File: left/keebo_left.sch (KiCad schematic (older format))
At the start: 57 parts, among them J0 Conn_01x01, SW1 SW_Push, SW10 SW_Push, SW11 SW_Push, SW12 SW_Push, SW13 SW_Push, SW14 SW_Push, SW17 SW_Push, SW18 SW_Push, SW19 SW_Push, SW2 SW_Push, SW20 SW_Push, SW21 SW_Push, SW22 SW_Push, SW25 SW_Push, SW26 SW_Push, SW27 SW_Push, SW28 SW_Push, SW29 SW_Push, SW3 SW_Push, SW30 SW_Push, SW35 SW_Push, SW36 SW_Push, SW37 SW_Push, SW4 SW_Push, SW5 SW_Push, SW6 SW_Push, SW7 SW_Push, SW9 SW_Push

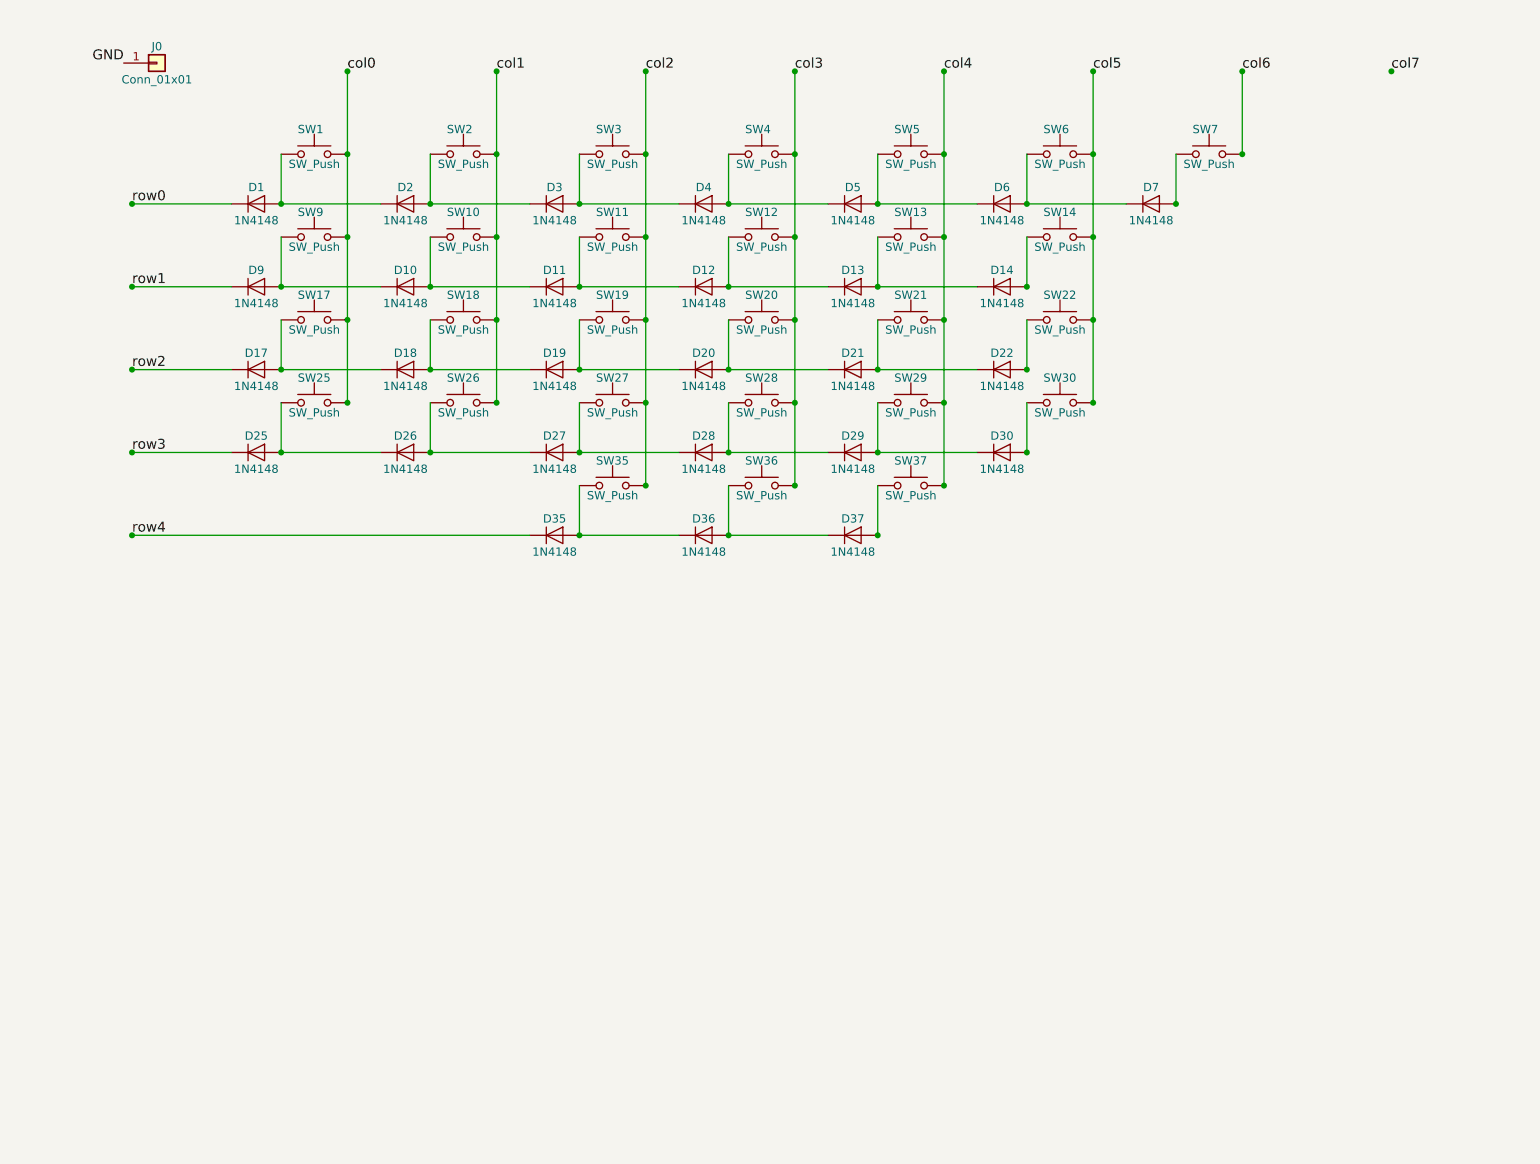
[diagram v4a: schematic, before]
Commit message: Create left board using new switch footprints
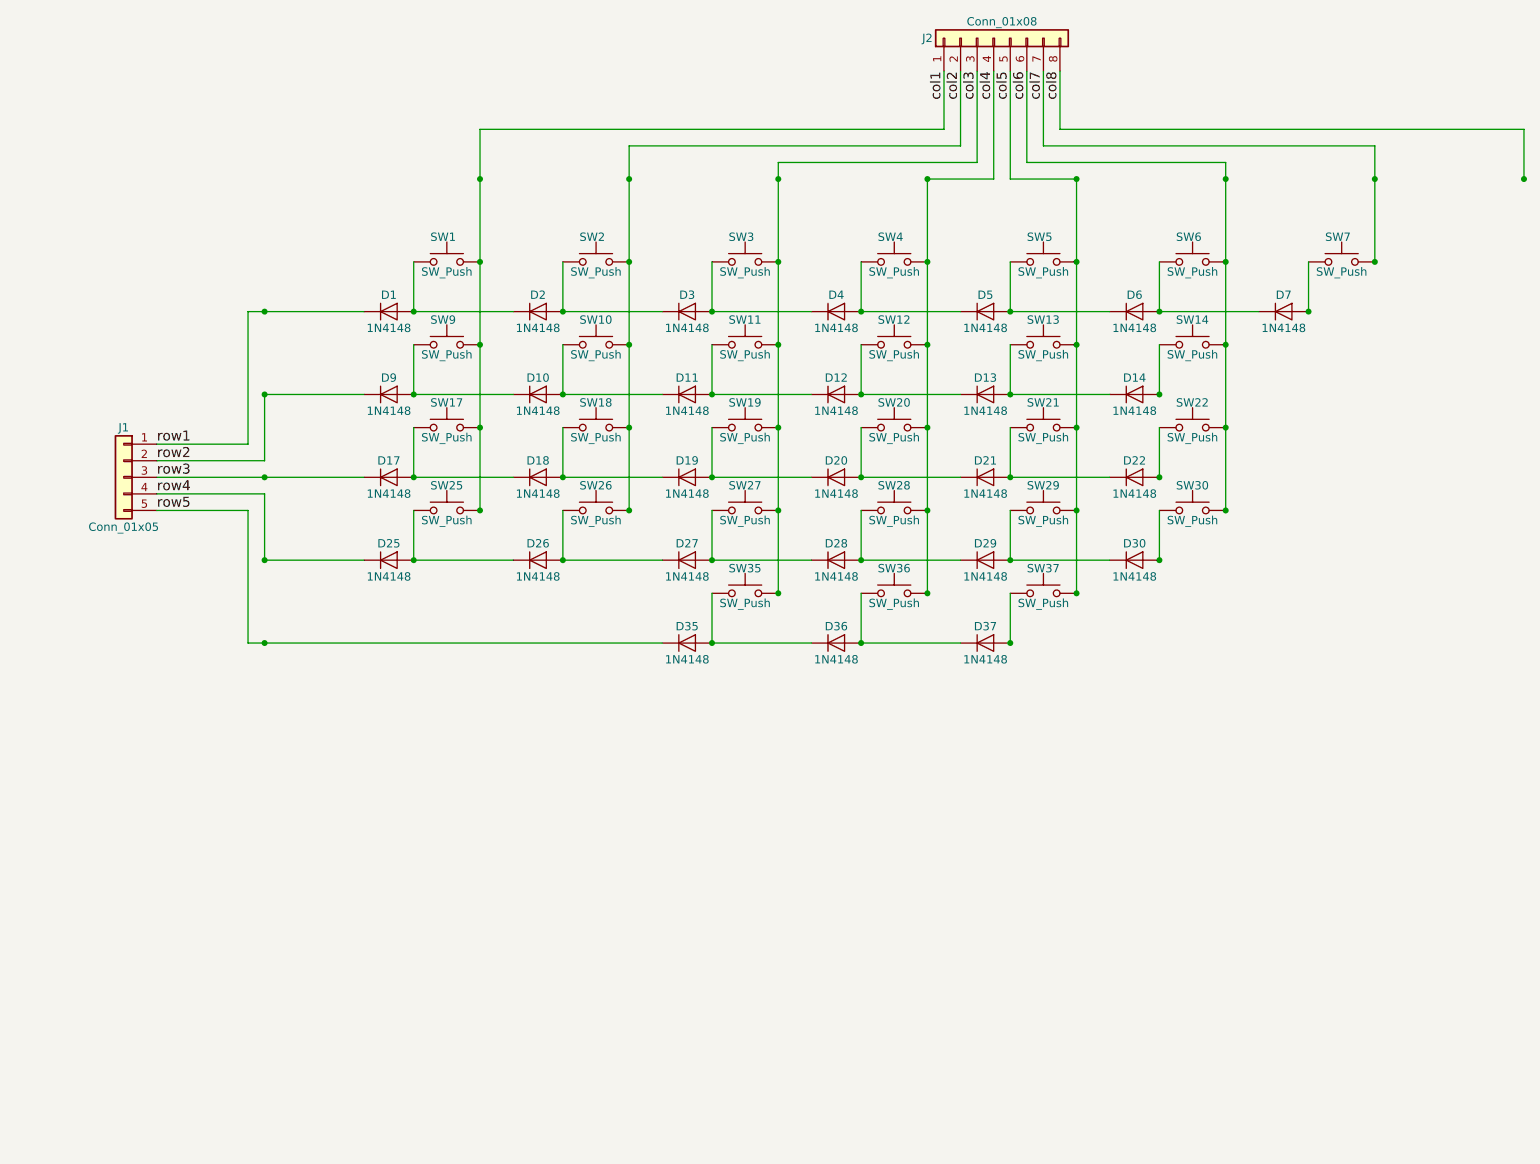
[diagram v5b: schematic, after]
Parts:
- removed J0: Conn_01x01, Mounting_Holes:MountingHole_3mm_Pad, symbol Conn_01x01
- added J1: Conn_01x05, kbo_pads:2mm_Pads_01x05, symbol Conn_01x05
- added J2: Conn_01x08, kbo_pads:2mm_Pads_01x08, symbol Conn_01x08
- SW1, SW10, SW11, SW12, SW13, SW14, SW18, SW19, SW2, SW20, SW21, SW22, SW26, SW27, SW28, SW29, SW3, SW30, SW4, SW5, SW6, SW7: footprint req:Mx_Alps_100 -> kbo_mx_lp_3d:KeeboHR_100_MX_LP
- SW17: footprint req:Mx_Alps_175 -> kbo_mx_lp_3d:KeeboHR_175_MX_LP
- SW25: footprint req:Mx_Alps_225 -> kbo_mx_lp_3d:KeeboHR_225_MX_LP
- SW35, SW36, SW37: footprint req:Mx_Alps_125 -> kbo_mx_lp_3d:KeeboHR_125_MX_LP
- SW9: footprint req:Mx_Alps_150 -> kbo_mx_lp_3d:KeeboHR_150_MX_LP
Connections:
- net col0 is gone; now on net col1: SW1.2, SW17.2, SW25.2, SW9.2
- net row0 is gone; now on net row1: D1.1 (K)
- net col1: now also J2.1 (Pin_1); no longer SW10.2, SW18.2, SW2.2, SW26.2
- net col2: now also SW10.2, SW18.2, SW2.2, SW26.2, J2.2 (Pin_2); no longer SW11.2, SW19.2, SW27.2, SW3.2, SW35.2
- net col3: now also SW11.2, SW19.2, SW27.2, SW3.2, SW35.2, J2.3 (Pin_3); no longer SW12.2, SW20.2, SW28.2, SW36.2, SW4.2
- net col4: now also SW12.2, SW20.2, SW28.2, SW36.2, SW4.2, J2.4 (Pin_4); no longer SW13.2, SW21.2, SW29.2, SW37.2, SW5.2
- net col5: now also SW13.2, SW21.2, SW29.2, SW37.2, SW5.2, J2.5 (Pin_5); no longer SW14.2, SW22.2, SW30.2, SW6.2
- net col6: now also SW14.2, SW22.2, SW30.2, SW6.2, J2.6 (Pin_6); no longer SW7.2
- net col7: now also SW7.2, J2.7 (Pin_7)
- net row1: now also J1.1 (Pin_1); no longer D9.1 (K)
- net row2: now also D9.1 (K), J1.2 (Pin_2); no longer D17.1 (K)
- net row3: now also D17.1 (K), J1.3 (Pin_3); no longer D25.1 (K)
- net row4: now also D25.1 (K), J1.4 (Pin_4); no longer D35.1 (K)
- new net col8: J2.8 (Pin_8)
- new net row5: D35.1 (K), J1.5 (Pin_5)
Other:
- moved on the sheet: D1, D10, D11, D12, D13, D14, D17, D18, D19, D2, D20, D21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

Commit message: Fix key matrix; use MX exclusively; Fix MX missing side holes.
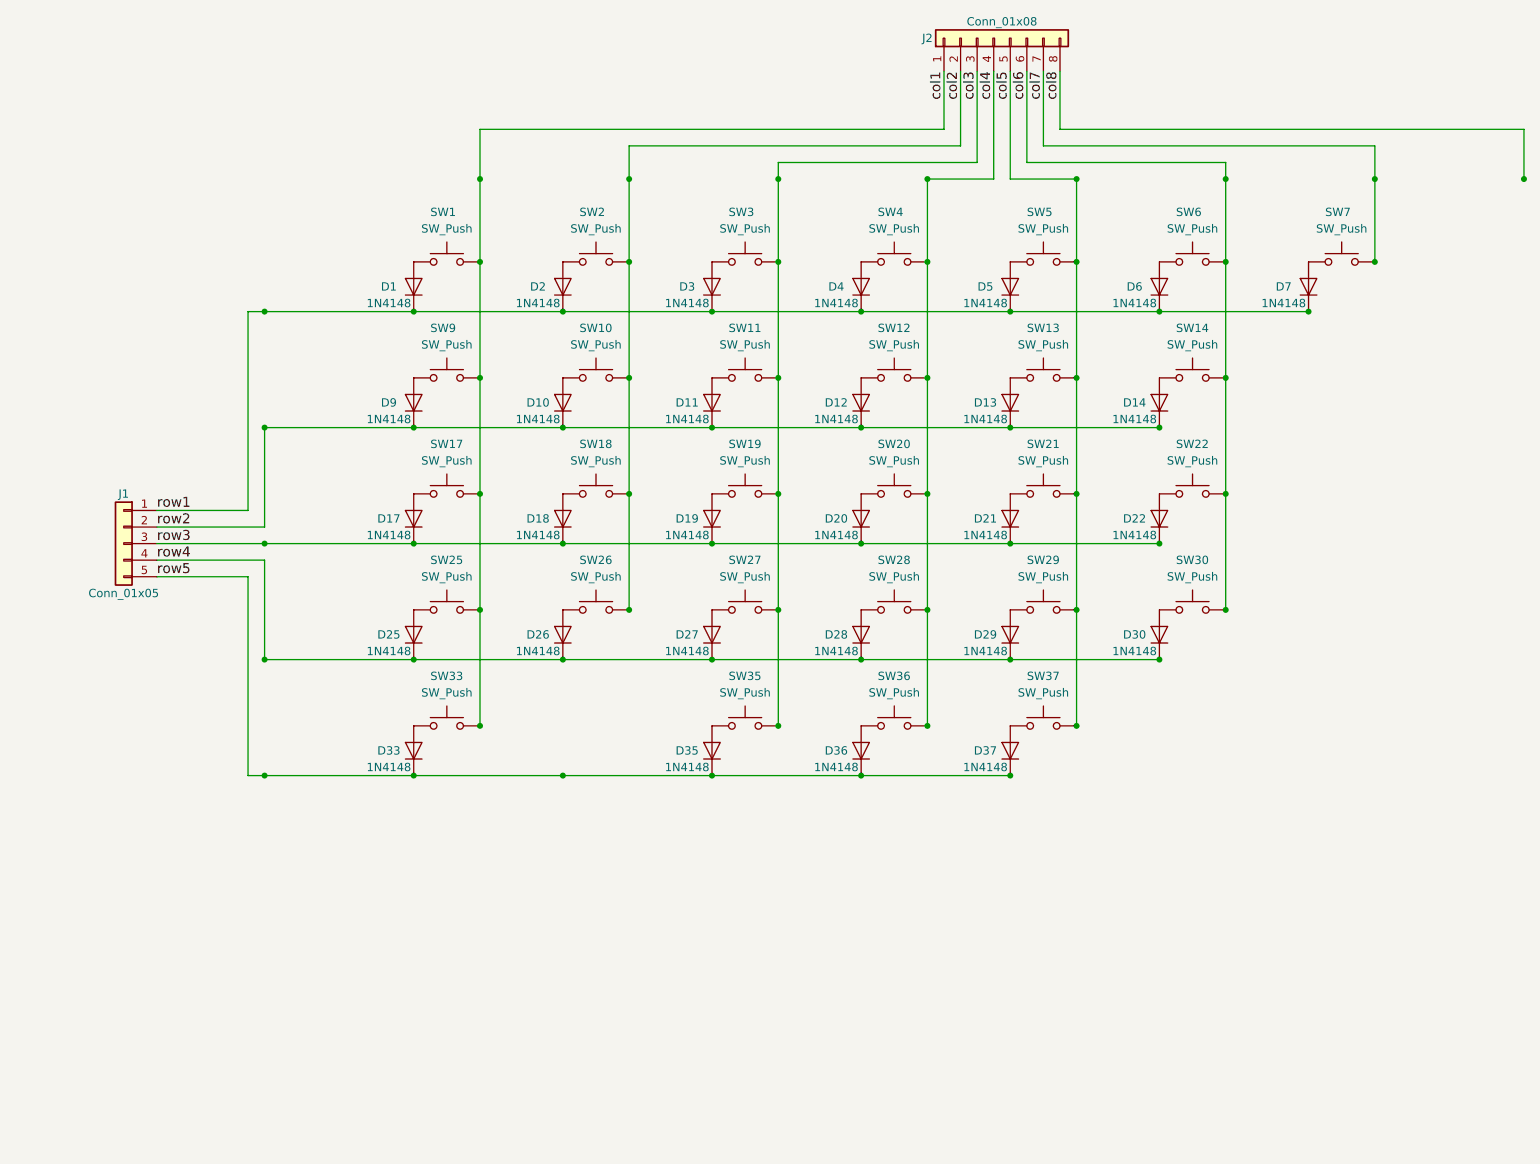
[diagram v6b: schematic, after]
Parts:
- added D33: 1N4148, Diodes_THT:D_DO-35_SOD27_P2.54mm_Vertical_AnodeUp, symbol 1N4148
- added SW33: SW_Push, kbo_mx_3d:KeeboHR_125_MX, symbol SW_Push
- D1, D10, D11, D12, D13, D14, D17, D18, D19, D2, D20, D21, D22, D25, D26, D27, D28, D29, D3, D30, D35, D36, D37, D4, D5, D6, D7, D9: footprint Diodes_SMD:D_SOD-123 -> Diodes_THT:D_DO-35_SOD27_P2.54mm_Vertical_AnodeUp
- SW1, SW10, SW11, SW12, SW13, SW14, SW18, SW19, SW2, SW20, SW21, SW22, SW26, SW27, SW28, SW29, SW3, SW30, SW4, SW5, SW6, SW7: footprint kbo_mx_lp_3d:KeeboHR_100_MX_LP -> kbo_mx_3d:KeeboHR_100_MX
- SW17: footprint kbo_mx_lp_3d:KeeboHR_175_MX_LP -> kbo_mx_3d:KeeboHR_175_MX
- SW25: footprint kbo_mx_lp_3d:KeeboHR_225_MX_LP -> kbo_mx_3d:KeeboHR_225_MX
- SW35, SW36, SW37: footprint kbo_mx_lp_3d:KeeboHR_125_MX_LP -> kbo_mx_3d:KeeboHR_125_MX
- SW9: footprint kbo_mx_lp_3d:KeeboHR_150_MX_LP -> kbo_mx_3d:KeeboHR_150_MX
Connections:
- net col1: now also SW33.2
- net row1: now also D2.1 (K), D3.1 (K), D4.1 (K), D5.1 (K), D6.1 (K), D7.1 (K)
- net row2: now also D10.1 (K), D11.1 (K), D12.1 (K), D13.1 (K), D14.1 (K)
- net row3: now also D18.1 (K), D19.1 (K), D20.1 (K), D21.1 (K), D22.1 (K)
- net row4: now also D26.1 (K), D27.1 (K), D28.1 (K), D29.1 (K), D30.1 (K)
- net row5: now also D36.1 (K), D37.1 (K), D33.1 (K)
- net at D1.2 (A), SW1.1: no longer D2.1 (K)
- net at D2.2 (A), SW2.1: no longer D3.1 (K)
- net at D3.2 (A), SW3.1: no longer D4.1 (K)
- net at D4.2 (A), SW4.1: no longer D5.1 (K)
- net at D5.2 (A), SW5.1: no longer D6.1 (K)
- net at D6.2 (A), SW6.1: no longer D7.1 (K)
- net at D9.2 (A), SW9.1: no longer D10.1 (K)
- net at D10.2 (A), SW10.1: no longer D11.1 (K)
- net at D11.2 (A), SW11.1: no longer D12.1 (K)
- net at D12.2 (A), SW12.1: no longer D13.1 (K)
- net at D13.2 (A), SW13.1: no longer D14.1 (K)
- net at D17.2 (A), SW17.1: no longer D18.1 (K)
- net at D18.2 (A), SW18.1: no longer D19.1 (K)
- net at D19.2 (A), SW19.1: no longer D20.1 (K)
- net at D20.2 (A), SW20.1: no longer D21.1 (K)
- net at D21.2 (A), SW21.1: no longer D22.1 (K)
- net at D25.2 (A), SW25.1: no longer D26.1 (K)
- net at D26.2 (A), SW26.1: no longer D27.1 (K)
- net at D27.2 (A), SW27.1: no longer D28.1 (K)
- net at D28.2 (A), SW28.1: no longer D29.1 (K)
- net at D29.2 (A), SW29.1: no longer D30.1 (K)
- net at D35.2 (A), SW35.1: no longer D36.1 (K)
- net at D36.2 (A), SW36.1: no longer D37.1 (K)
- new net: D33.2 (A), SW33.1
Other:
- moved on the sheet: D1, J1
